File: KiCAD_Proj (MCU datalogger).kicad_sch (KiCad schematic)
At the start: 5 parts, among them U1 ATMEGA328P-AU, U2 DS1337S_, U3 24LC1025-I_SM, U4 24LC1025-I_SM

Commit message: Test: made a small schematic change
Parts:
- added R2, R3: R, symbol Device:R
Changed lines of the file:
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@@
+	)
+	(symbol
+		(lib_id "Device:R")
+		(at 172.72 118.11 0)
+		(unit 1)
+		(exclude_from_sim no)
+		(in_bom yes)
+		(on_board yes)
+		(dnp no)
+		(fields_autoplaced yes)
+		(property "Reference" "R2"
+			(at 175.26 116.8399 0)
+			(effects
+				(font
+					(size 1.27 1.27)
+				)
+				(justify left)
+			)
+		)
+		(property "Value" "R"
+			(at 175.26 119.3799 0)
+			(effects
+				(font
+					(size 1.27 1.27)
+				)
+				(justify left)
+			)
+		)
+		(property "Footprint" ""
+			(at 170.942 118.11 90)
+			(effects
+				(font
+					(size 1.27 1.27)
+				)
+				(hide yes)
+			)
+		)
+		(property "Datasheet" "~"
+			(at 172.72 118.11 0)
+			(effects
+				(font
+					(size 1.27 1.27)
+				)
+				(hide yes)
+			)
+		)
+		(property "Description" "Resistor"
+			(at 172.72 118.11 0)
+			(effects
+				(font
+					(size 1.27 1.27)
+				)
+				(hide yes)
+			)
+		)
+		(pin "2"
+		)
+		(pin "1"
+		)
+		(instances
+			(project ""
+				(path "/4bd39814-648a-43e5-9d59-9775154104be"
+					(reference "R2")
+					(unit 1)
+				)
+			)
+		)
 	)
 	(symbol
@@
 					(unit 1)
 				)
+			)
+		)
+	)
+	(symbol
+		(lib_id "Device:R")
+		(at 187.96 118.11 0)
+		(unit 1)
+		(exclude_from_sim no)
+		(in_bom yes)
+		(on_board yes)
+		(dnp no)
+		(fields_autoplaced yes)
+		(property "Reference" "R3"
+			(at 190.5 116.8399 0)
+			(effects
+				(font
+					(size 1.27 1.27)
+				)
+				(justify left)
+			)
+		)
+		(property "Value" "R"
+			(at 190.5 119.3799 0)
+			(effects
+				(font
+					(size 1.27 1.27)
+				)
+				(justify left)
+			)
+		)
+		(property "Footprint" ""
+			(at 186.182 118.11 90)
+			(effects
+				(font
+					(size 1.27 1.27)
+				)
+				(hide yes)
+			)
+		)
+		(property "Datasheet" "~"
+			(at 187.96 118.11 0)
+			(effects
+				(font
+					(size 1.27 1.27)
+				)
+				(hide yes)
+			)
+		)
+		(property "Description" "Resistor"
+			(at 187.96 118.11 0)
+			(effects
+				(font
+					(size 1.27 1.27)
+				)
+				(hide yes)
+			)
+		)
+		(pin "2"
+		)
+		(pin "1"
+		)
+		(instances
+			(project ""
+				(path "/4bd39814-648a-43e5-9d59-9775154104be"
+					(reference "R3")
+					(unit 1)
+				)

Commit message: Test: made a small schematic change
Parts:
- removed R2, R3: R, symbol Device:R
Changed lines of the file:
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@@
 	(paper "A4")
+	(symbol
+		(lib_id "Device:R")
+		(at 170.18 114.3 0)
+		(unit 1)
+		(exclude_from_sim no)
+		(in_bom yes)
+		(on_board yes)
+		(dnp no)
+		(fields_autoplaced yes)
+		(property "Reference" "R1"
+			(at 172.72 113.0299 0)
+			(effects
+				(font
+					(size 1.27 1.27)
+				)
+				(justify left)
+			)
+		)
+		(property "Value" "R"
+			(at 172.72 115.5699 0)
+			(effects
+				(font
+					(size 1.27 1.27)
+				)
+				(justify left)
+			)
+		)
+		(property "Footprint" ""
+			(at 168.402 114.3 90)
+			(effects
+				(font
+					(size 1.27 1.27)
+				)
+				(hide yes)
+			)
+		)
+		(property "Datasheet" "~"
+			(at 170.18 114.3 0)
+			(effects
+				(font
+					(size 1.27 1.27)
+				)
+				(hide yes)
+			)
+		)
+		(property "Description" "Resistor"
+			(at 170.18 114.3 0)
+			(effects
+				(font
+					(size 1.27 1.27)
+				)
+				(hide yes)
+			)
+		)
+		(pin "2"
+		)
+		(pin "1"
+		)
+		(instances
+			(project ""
+				(path "/4bd39814-648a-43e5-9d59-9775154104be"
+					(reference "R1")
+					(unit 1)
+				)
+			)
+		)
+	)
 	(symbol
 		(lib_id "24LC1025-I_SM:24LC1025-I_SM")
@@
 	)
 	(symbol
-		(lib_id "Device:R")
-		(at 172.72 118.11 0)
-		(unit 1)
-		(exclude_from_sim no)
-		(in_bom yes)
-		(on_board yes)
-		(dnp no)
-		(fields_autoplaced yes)
-		(property "Reference" "R2"
-			(at 175.26 116.8399 0)
-			(effects
-				(font
-					(size 1.27 1.27)
-				)
-				(justify left)
-			)
-		)
-		(property "Value" "R"
-			(at 175.26 119.3799 0)
-			(effects
-				(font
-					(size 1.27 1.27)
-				)
-				(justify left)
-			)
-		)
-		(property "Footprint" ""
-			(at 170.942 118.11 90)
-			(effects
-				(font
-					(size 1.27 1.27)
-				)
-				(hide yes)
-			)
-		)
-		(property "Datasheet" "~"
-			(at 172.72 118.11 0)
-			(effects
-				(font
-					(size 1.27 1.27)
-				)
-				(hide yes)
-			)
-		)
-		(property "Description" "Resistor"
-			(at 172.72 118.11 0)
-			(effects
-				(font
-					(size 1.27 1.27)
-				)
-				(hide yes)
-			)
-		)
-		(pin "2"
-		)
-		(pin "1"
-		)
-		(instances
-			(project ""
-				(path "/4bd39814-648a-43e5-9d59-9775154104be"
-					(reference "R2")
-					(unit 1)
-				)
-			)
-		)
-	)
-	(symbol
 		(lib_id "DS1337S:DS1337S_")
 		(at 46.99 73.66 0)
@@
 					(unit 1)
 				)
-			)
-		)
-	)
-	(symbol
-		(lib_id "Device:R")
-		(at 187.96 118.11 0)
-		(unit 1)
-		(exclude_from_sim no)
-		(in_bom yes)
-		(on_board yes)
-		(dnp no)
-		(fields_autoplaced yes)
-		(property "Reference" "R3"
-			(at 190.5 116.8399 0)
-			(effects
-				(font
-					(size 1.27 1.27)
-				)
-				(justify left)
-			)
-		)
-		(property "Value" "R"
-			(at 190.5 119.3799 0)
-			(effects
-				(font
-					(size 1.27 1.27)
-				)
-				(justify left)
-			)
-		)
-		(property "Footprint" ""
-			(at 186.182 118.11 90)
-			(effects
-				(font
-					(size 1.27 1.27)
-				)
-				(hide yes)
-			)
-		)
-		(property "Datasheet" "~"
-			(at 187.96 118.11 0)
-			(effects
-				(font
-					(size 1.27 1.27)
-				)
-				(hide yes)
-			)
-		)
-		(property "Description" "Resistor"
-			(at 187.96 118.11 0)
-			(effects
-				(font
-					(size 1.27 1.27)
-				)
-				(hide yes)
-			)
-		)
-		(pin "2"
-		)
-		(pin "1"
-		)
-		(instances
-			(project ""
-				(path "/4bd39814-648a-43e5-9d59-9775154104be"
-					(reference "R3")
-					(unit 1)
-				)
-			)
-		)
-	)
-	(symbol
-		(lib_id "Device:R")
-		(at 160.02 119.38 0)
-		(unit 1)
-		(exclude_from_sim no)
-		(in_bom yes)
-		(on_board yes)
-		(dnp no)
-		(fields_autoplaced yes)
-		(property "Reference" "R1"
-			(at 162.56 118.1099 0)
-			(effects
-				(font
-					(size 1.27 1.27)
-				)
-				(justify left)
-			)
-		)
-		(property "Value" "R"
-			(at 162.56 120.6499 0)
-			(effects
-				(font
-					(size 1.27 1.27)
-				)
-				(justify left)
-			)
-		)
-		(property "Footprint" ""
-			(at 158.242 119.38 90)
-			(effects
-				(font
-					(size 1.27 1.27)
-				)
-				(hide yes)
-			)
-		)
-		(property "Datasheet" "~"
-			(at 160.02 119.38 0)
-			(effects
-				(font
-					(size 1.27 1.27)
-				)
-				(hide yes)
-			)
-		)
-		(property "Description" "Resistor"
-			(at 160.02 119.38 0)
-			(effects
-				(font
-					(size 1.27 1.27)
-				)
-				(hide yes)
-			)
-		)
-		(pin "1"
-		)
-		(pin "2"
-		)
-		(instances
-			(project ""
-				(path "/4bd39814-648a-43e5-9d59-9775154104be"
-					(reference "R1")
-					(unit 1)
-				)

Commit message: Test: made a small schematic change
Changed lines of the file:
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@@
 	(paper "A4")
-	(symbol
-		(lib_id "Device:R")
-		(at 170.18 114.3 0)
-		(unit 1)
-		(exclude_from_sim no)
-		(in_bom yes)
-		(on_board yes)
-		(dnp no)
-		(fields_autoplaced yes)
-		(property "Reference" "R1"
-			(at 172.72 113.0299 0)
-			(effects
-				(font
-					(size 1.27 1.27)
-				)
-				(justify left)
-			)
-		)
-		(property "Value" "R"
-			(at 172.72 115.5699 0)
-			(effects
-				(font
-					(size 1.27 1.27)
-				)
-				(justify left)
-			)
-		)
-		(property "Footprint" ""
-			(at 168.402 114.3 90)
-			(effects
-				(font
-					(size 1.27 1.27)
-				)
-				(hide yes)
-			)
-		)
-		(property "Datasheet" "~"
-			(at 170.18 114.3 0)
-			(effects
-				(font
-					(size 1.27 1.27)
-				)
-				(hide yes)
-			)
-		)
-		(property "Description" "Resistor"
-			(at 170.18 114.3 0)
-			(effects
-				(font
-					(size 1.27 1.27)
-				)
-				(hide yes)
-			)
-		)
-		(pin "2"
-		)
-		(pin "1"
-		)
-		(instances
-			(project ""
-				(path "/4bd39814-648a-43e5-9d59-9775154104be"
-					(reference "R1")
-					(unit 1)
-				)
-			)
-		)
-	)
 	(symbol
 		(lib_id "24LC1025-I_SM:24LC1025-I_SM")
@@
 					(unit 1)
 				)
+			)
+		)
+	)
+	(symbol
+		(lib_id "Device:R")
+		(at 180.34 120.65 0)
+		(unit 1)
+		(exclude_from_sim no)
+		(in_bom yes)
+		(on_board yes)
+		(dnp no)
+		(fields_autoplaced yes)
+		(property "Reference" "R1"
+			(at 182.88 119.3799 0)
+			(effects
+				(font
+					(size 1.27 1.27)
+				)
+				(justify left)
+			)
+		)
+		(property "Value" "R"
+			(at 182.88 121.9199 0)
+			(effects
+				(font
+					(size 1.27 1.27)
+				)
+				(justify left)
+			)
+		)
+		(property "Footprint" ""
+			(at 178.562 120.65 90)
+			(effects
+				(font
+					(size 1.27 1.27)
+				)
+				(hide yes)
+			)
+		)
+		(property "Datasheet" "~"
+			(at 180.34 120.65 0)
+			(effects
+				(font
+					(size 1.27 1.27)
+				)
+				(hide yes)
+			)
+		)
+		(property "Description" "Resistor"
+			(at 180.34 120.65 0)
+			(effects
+				(font
+					(size 1.27 1.27)
+				)
+				(hide yes)
+			)
+		)
+		(pin "2"
+		)
+		(pin "1"
+		)
+		(instances
+			(project ""
+				(path "/4bd39814-648a-43e5-9d59-9775154104be"
+					(reference "R1")
+					(unit 1)
+				)

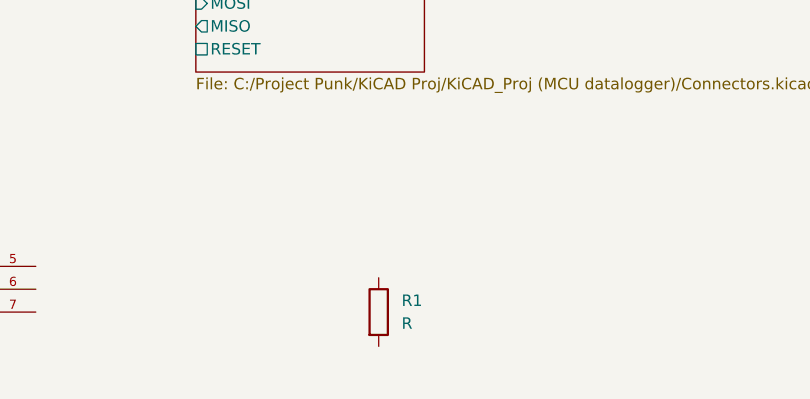
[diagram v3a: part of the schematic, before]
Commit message: Added Resistor to schematic
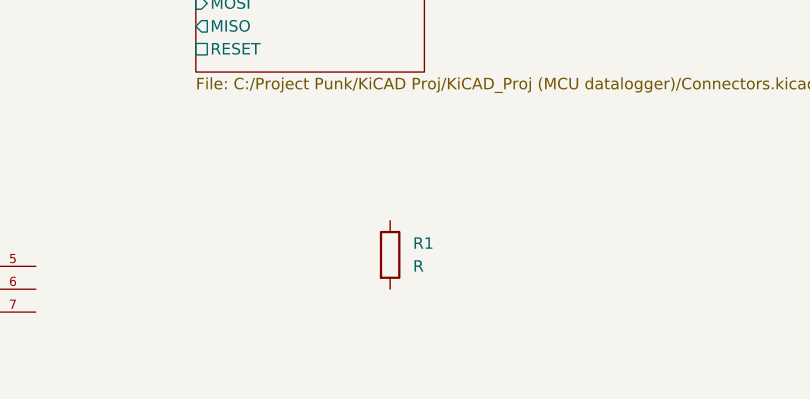
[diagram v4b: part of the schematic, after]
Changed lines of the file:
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@@
 	(symbol
 		(lib_id "Device:R")
-		(at 180.34 120.65 0)
+		(at 181.61 114.3 0)
 		(unit 1)
 		(exclude_from_sim no)
@@
 		(fields_autoplaced yes)
 		(property "Reference" "R1"
-			(at 182.88 119.3799 0)
+			(at 184.15 113.0299 0)
 			(effects
 				(font
@@
 		)
 		(property "Value" "R"
-			(at 182.88 121.9199 0)
+			(at 184.15 115.5699 0)
 			(effects
 				(font
@@
 		)
 		(property "Footprint" ""
-			(at 178.562 120.65 90)
+			(at 179.832 114.3 90)
 			(effects
 				(font
@@
 		)
 		(property "Datasheet" "~"
-			(at 180.34 120.65 0)
+			(at 181.61 114.3 0)
 			(effects
 				(font
@@
 		)
 		(property "Description" "Resistor"
-			(at 180.34 120.65 0)
+			(at 181.61 114.3 0)
 			(effects
 				(font

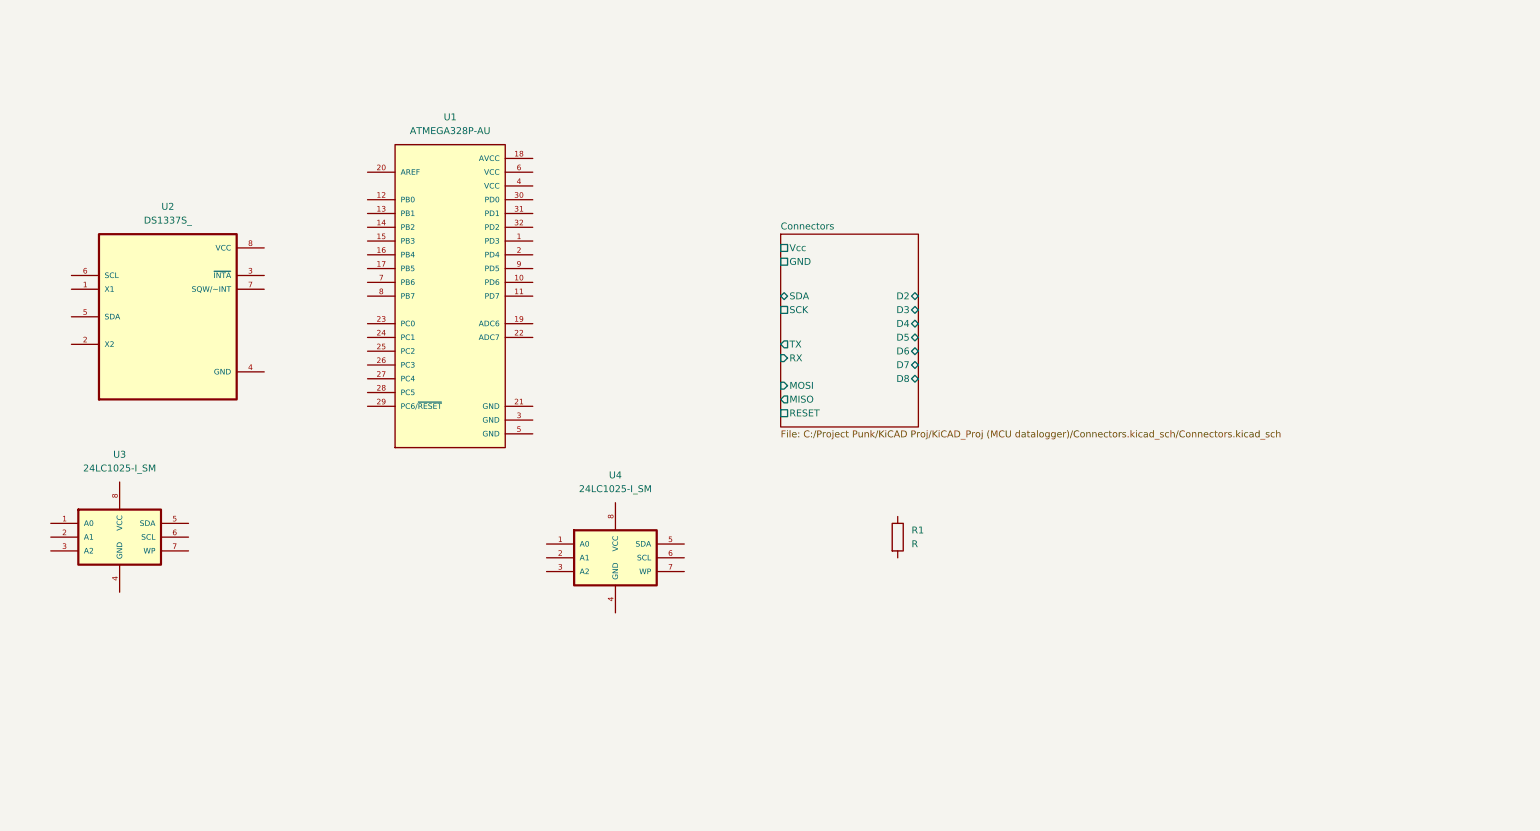
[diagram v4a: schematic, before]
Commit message: Have added required symbols to the schematic sheets.
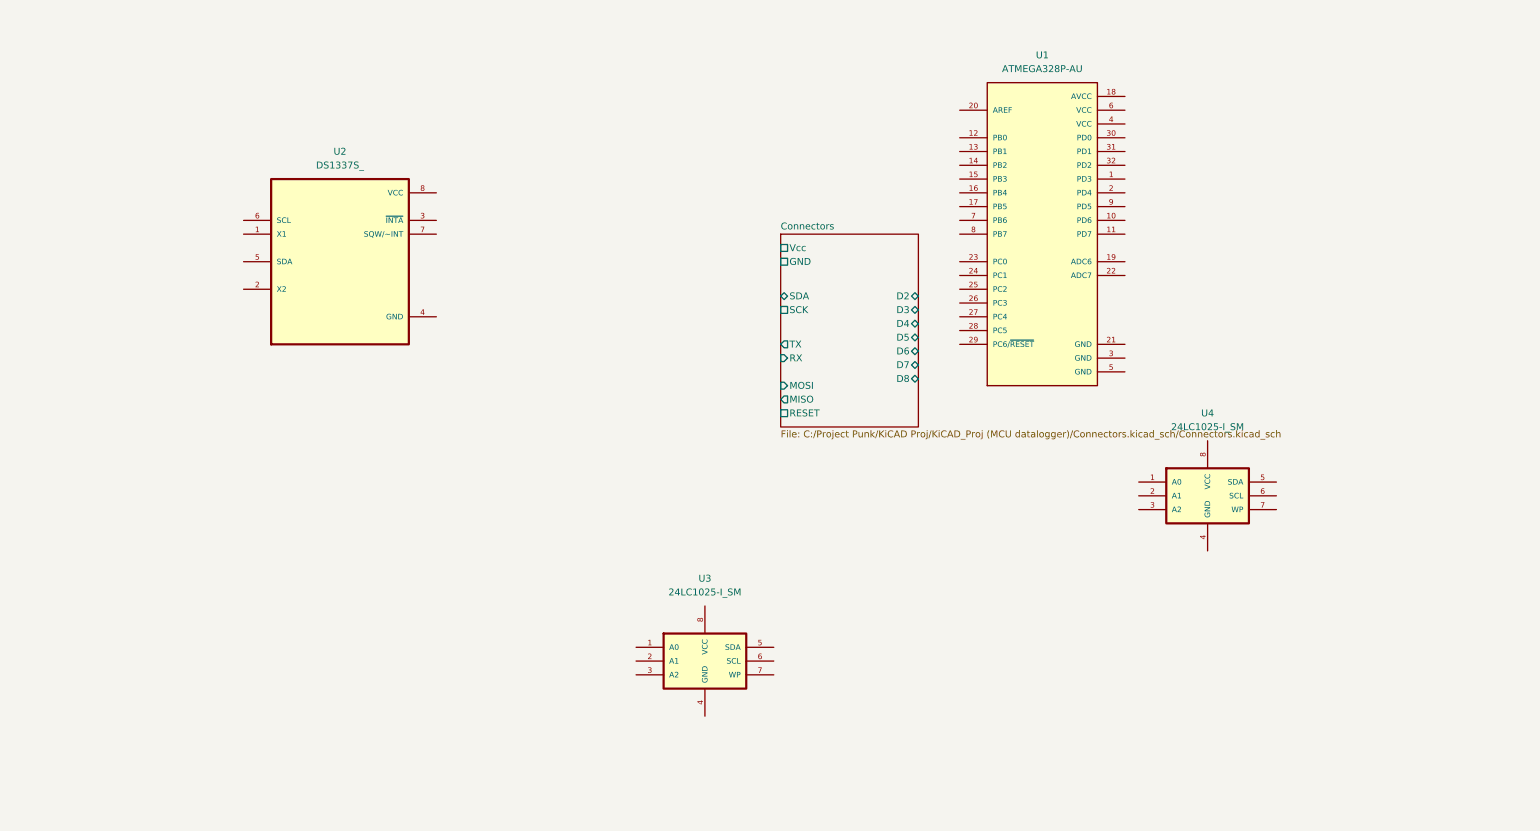
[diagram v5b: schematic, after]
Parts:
- removed R1: R, symbol Device:R
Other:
- moved on the sheet: U1, U2, U3, U4

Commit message: Added component values.
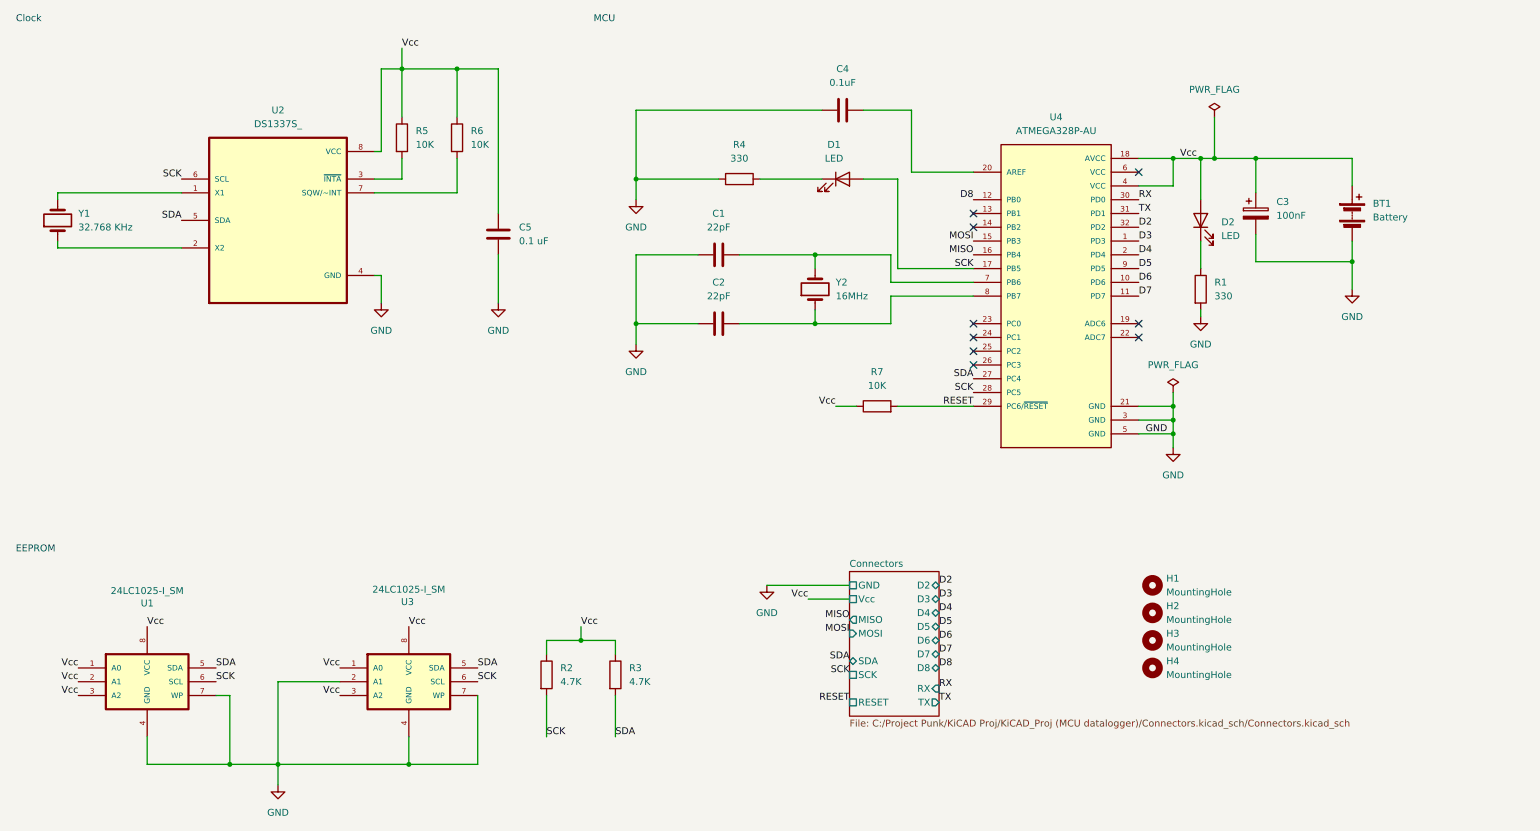
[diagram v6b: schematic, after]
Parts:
- removed U2: DS1337S_, DS1337S_:SOIC127P600X175-8N, symbol DS1337S:DS1337S_
- added BT1: Battery, symbol Device:Battery
- added C1, C2: 22pF, symbol Device:C
- added C3: 100nF, symbol Device:C_Polarized
- added C4: 0.1uF, symbol Device:C
- added C5: 0.1 uF, symbol Device:C
- added D1, D2: LED, symbol Device:LED
- added H1, H2, H3, H4: MountingHole, symbol Mechanical:MountingHole
- added R1, R4: 330, symbol Device:R
- added R2, R3: 4.7K, symbol Device:R
- added R5, R6, R7: 10K, symbol Device:R
- added U2: DS1337S_, DS1337S_:SOIC127P600X175-8N, symbol DS1337S_:DS1337S_
- added Y1: 32.768 KHz, symbol Device:Crystal
- added Y2: 16MHz, symbol Device:Crystal
- renumbered U4 to U1, U1 to U4
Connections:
- net Vcc: now reaches U1.1 (A0)
- net Vcc: now also U1.2 (A1), U1.3 (A2), U1.8 (VCC), U3.1 (A0), U3.3 (A2), U3.8 (VCC), U4.18 (AVCC), U4.4 (VCC), BT1.1 (+), C3.1, C5.1, D2.2 (A), R2.1, R3.1, R5.1, R6.1, R7.1, U2.8 (VCC)
- net GND: now reaches U1.4 (GND)
- net GND: now also U1.7 (WP), U3.2 (A1), U3.4 (GND), U3.7 (WP), U4.21 (GND), U4.3 (GND), U4.5 (GND), BT1.2 (-), C1.1, C2.1, C3.2, C4.1, C5.2, R1.2, R4.1, U2.4 (GND)
- net SDA: now reaches U1.5 (SDA)
- net SDA: now also U3.5 (SDA), U4.27 (PC4), R3.2, U2.5 (SDA)
- net SCK: now reaches U1.6 (SCL)
- net SCK: now also U3.6 (SCL), U4.17 (PB5), U4.28 (PC5), D1.2 (A), R2.2, U2.6 (SCL)
- net D3: now reaches U4.1 (PD3)
- net D6: now reaches U4.10 (PD6)
- net D7: now reaches U4.11 (PD7)
- net D8: now reaches U4.12 (PB0)
- net MOSI: now reaches U4.15 (PB3)
- net MISO: now reaches U4.16 (PB4)
- net D4: now reaches U4.2 (PD4)
- net at U4.20 (AREF): now also C4.2
- net RESET: now reaches U4.29 (PC6/~{RESET})
- net RESET: now also R7.2
- net RX: now reaches U4.30 (PD0)
- net TX: now reaches U4.31 (PD1)
- net D2: now reaches U4.32 (PD2)
- net at U4.7 (PB6): now also C1.2, Y2.2
- net at U4.8 (PB7): now also C2.2, Y2.1
- net D5: now reaches U4.9 (PD5)
- new net: R6.2, U2.7 (SQW/~INT)
- new net: U2.2 (X2), Y1.1
- new net: U2.1 (X1), Y1.2
- new net: R5.2, U2.3 (~{INTA})
- new net: D2.1 (K), R1.1
- new net: D1.1 (K), R4.2
- no-connect marks 0 -> 9
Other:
- note added: "Clock"
- note added: "EEPROM"
- note added: "MCU"
- moved on the sheet: U1, U3, U4
